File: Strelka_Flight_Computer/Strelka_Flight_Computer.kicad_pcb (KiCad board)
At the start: 4 copper layers, 91 x 30.1 mm, 174 parts, among them IC1 XTSD04GLGEAG, IC2 MAX-M10S-00B, J2 Conn_01x04, J3 DB125-3.5-4P-GN-S, J4 SM06B-GHS-TB(LF)(SN), J6 USB_B_Micro, J7 Conn_01x02, J8 Conn_01x07, Q1 CJK2333, Q10 AP2300, Q11 MMBT2222, Q15 AO3400A, Q16 AO3400A, Q17 AO3401A, Q2 CJK2333, Q4 AO3401A, Q5 AP2300, Q6 MMBT2222, Q9 AO3401A, SW1 SW_DIP_x01, SW6 TS-1185-C-A-A-A, SW7 TS-1185-C-A-A-A, U1 ASM330LHHXTR, U11 BMX055, U12 MS561101BA03-50, U16 TPS61085DGKR, U2 AP9101CK6, U3 AMS1117-3.3, U4 RFM95W-915S2, U5 MCP2551-I-SN, U6 STM32H743VITx, U8 USBLC6-2SC6, Y5 Q13FC1350000400, Y6 X1E0000210834

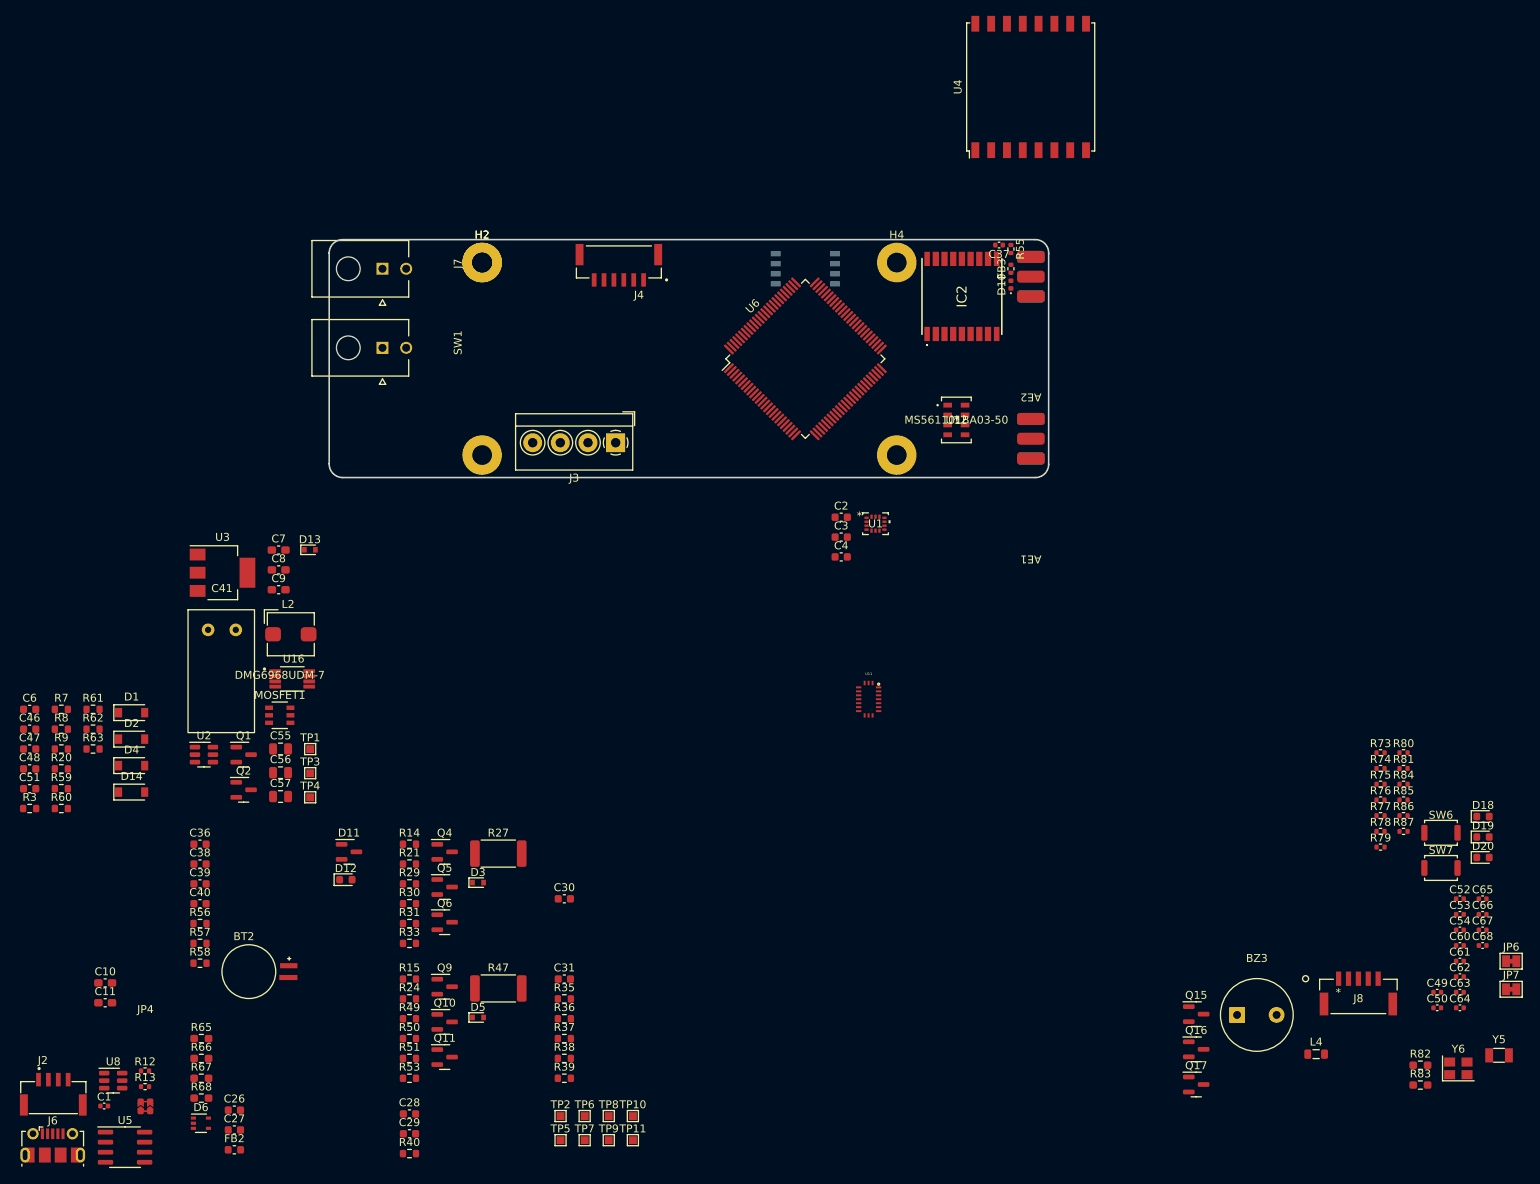
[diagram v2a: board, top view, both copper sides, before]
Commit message: Started component placement
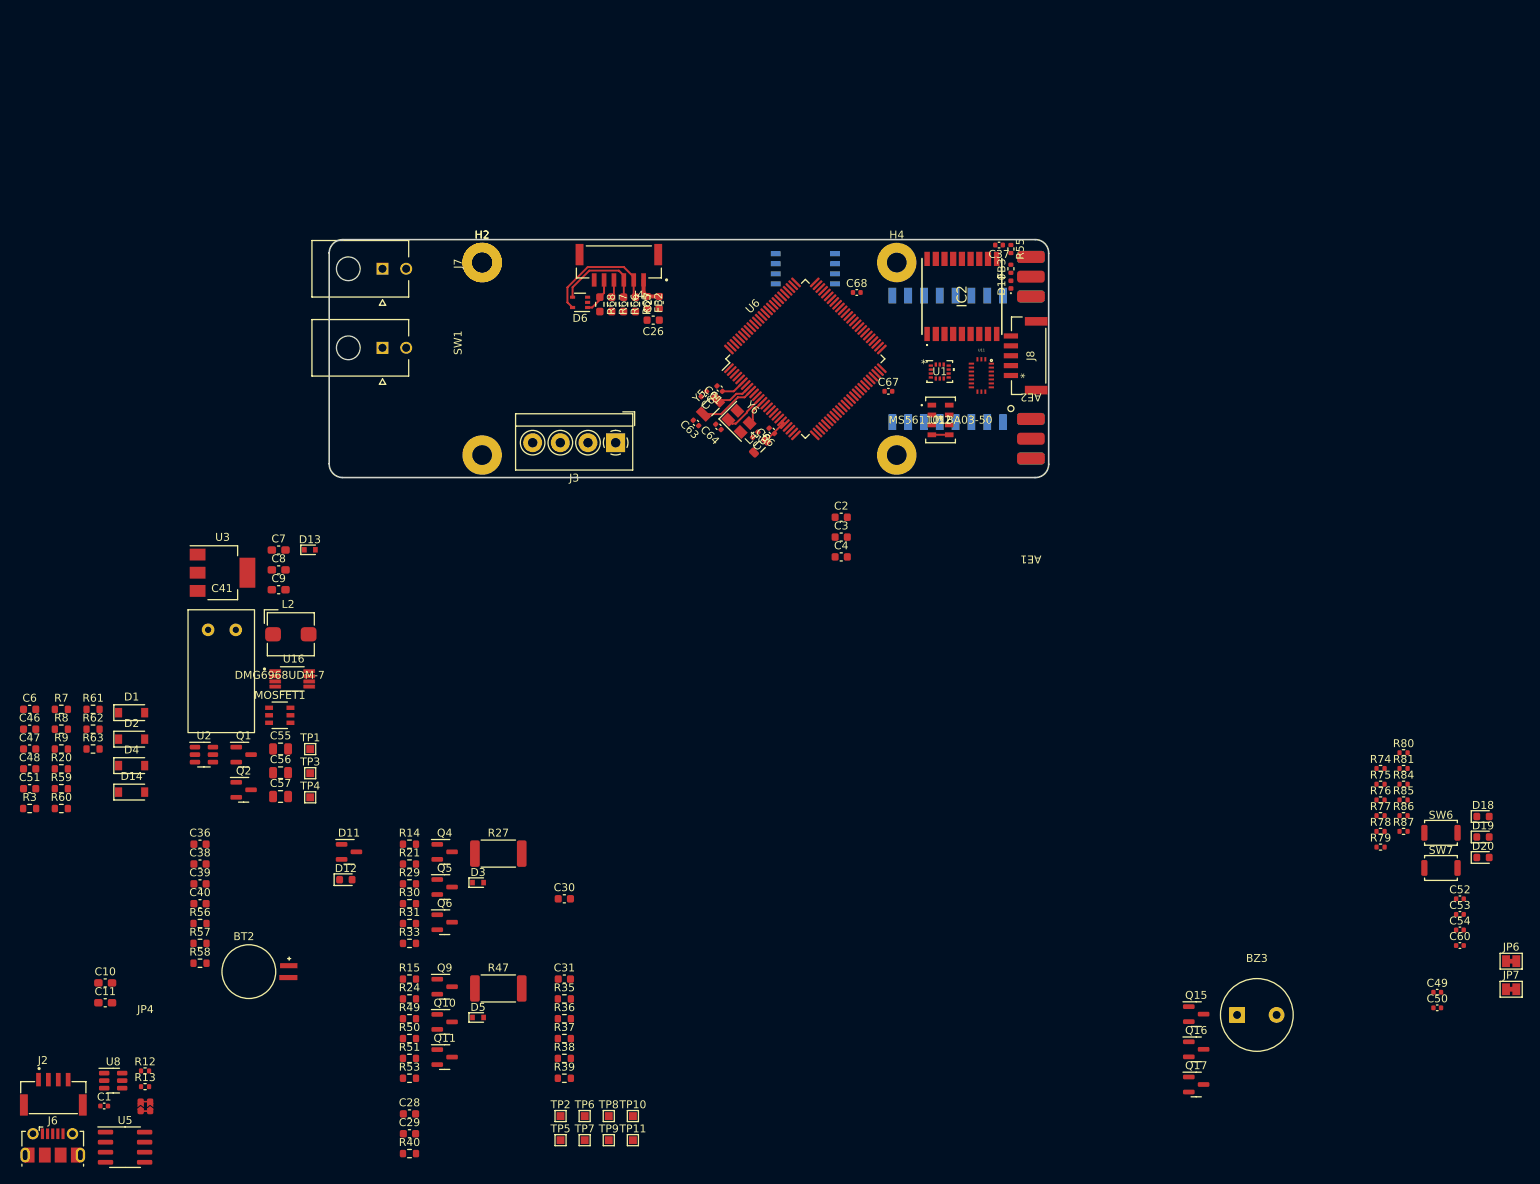
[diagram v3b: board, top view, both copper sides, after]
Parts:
- removed R73: 100k, Resistor_SMD:R_0402_1005Metric
- removed R82: NC, Resistor_SMD:R_0603_1608Metric_Pad0.98x0.95mm_HandSolder
- removed R83: 10k, Resistor_SMD:R_0603_1608Metric_Pad0.98x0.95mm_HandSolder
- U4: moved to B.Cu
- moved Y5 129.1 mm to (146.5, 69.5), turned to 45 degrees
- moved Y6 122.4 mm to (150.1, 71.3), turned to -45 degrees
- moved C62 120.7 mm to (145.7, 67.8), turned to -135 degrees
- moved C63 120.5 mm to (144.7, 71.5), turned to 135 degrees
- moved FB2 119.2 mm to (138.5, 56.3), turned to -90 degrees
- moved C64 119.2 mm to (147.5, 72.0), turned to 135 degrees
- moved C61 118.4 mm to (147.7, 67.2), turned to 135 degrees
- moved C27 117.7 mm to (140.0, 56.3), turned to 90 degrees
- moved C68 114.4 mm to (165.0, 55.0)
- moved D6 114.4 mm to (130.0, 56.2), turned to 180 degrees
- moved C26 113.1 mm to (139.2, 58.5), turned to 180 degrees
- moved R68 112.4 mm to (132.5, 56.5), turned to -90 degrees
- moved R67 110.8 mm to (134.0, 56.5), turned to -90 degrees
- moved R66 109.3 mm to (135.5, 56.5), turned to -90 degrees
- moved C65 109.1 mm to (152.2, 73.0), turned to -135 degrees
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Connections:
- C66 pad 1: Net-(U6-VDDA) -> /STM32H743/VDDA
- L4 pad 2: Net-(U6-VDDA) -> /STM32H743/VDDA
- U1 pad 4: /STM32H743/INT_IN4 -> /STM32H743/EXTI13
- U1 pad 9: /STM32H743/INT_IN5 -> /STM32H743/EXTI14
- U11 pad 14: /STM32H743/INT_IN2 -> /STM32H743/EXTI6
- U11 pad 19: /STM32H743/INT_IN1 -> /STM32H743/EXTI15
- U11 pad 2: /STM32H743/INT_IN3 -> /STM32H743/EXTI7
- U6 pad 15: unconnected-(U6-PC0-Pad15) -> GND
- U6 pad 21: Net-(U6-VDDA) -> /STM32H743/VDDA
- U6 pad 51: unconnected-(U6-PB12-Pad51) -> /915MHz_Radio/IO0_RF
- U6 pad 60: unconnected-(U6-PD13-Pad60) -> /STM32H743/EXTI13
- U6 pad 61: unconnected-(U6-PD14-Pad61) -> /STM32H743/EXTI14
- U6 pad 62: unconnected-(U6-PD15-Pad62) -> /STM32H743/EXTI15
- U6 pad 63: unconnected-(U6-PC6-Pad63) -> /STM32H743/EXTI6
- U6 pad 64: unconnected-(U6-PC7-Pad64) -> /STM32H743/EXTI7
- U6 pad 84: /STM32H743/INT_IN1 -> unconnected-(U6-PD3-Pad84)
- U6 pad 85: /STM32H743/INT_IN2 -> unconnected-(U6-PD4-Pad85)
- U6 pad 86: /STM32H743/INT_IN3 -> unconnected-(U6-PD5-Pad86)
- U6 pad 87: /STM32H743/INT_IN4 -> unconnected-(U6-PD6-Pad87)
- U6 pad 88: /STM32H743/INT_IN5 -> unconnected-(U6-PD7-Pad88)
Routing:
- net Net-(D6-K-Pad5): track 0.00 -> 15.4 mm
- net Net-(D6-K-Pad4): track 0.00 -> 11.6 mm
- net /STM32H743/OSC32_OUT: track 0.00 -> 7.28 mm
- net /STM32H743/OSC_IN: track 0.00 -> 5.52 mm
- net Net-(D6-K-Pad1): track 0.00 -> 4.69 mm
- net /STM32H743/OSC32_IN: track 0.00 -> 4.57 mm
- net /STM32H743/VDDA: track 0.00 -> 3.80 mm
- net Net-(C27-Pad2): track 0.00 -> 3.79 mm
- net /STM32H743/OSC_OUT: track 0.00 -> 3.36 mm
- net +3.3V: track 0.00 -> 3.08 mm
- net Net-(D6-K-Pad3): track 0.00 -> 2.30 mm
- net /STM32H743/SPI4_NSS: track 0.00 -> 2.20 mm

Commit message: Changed design rules
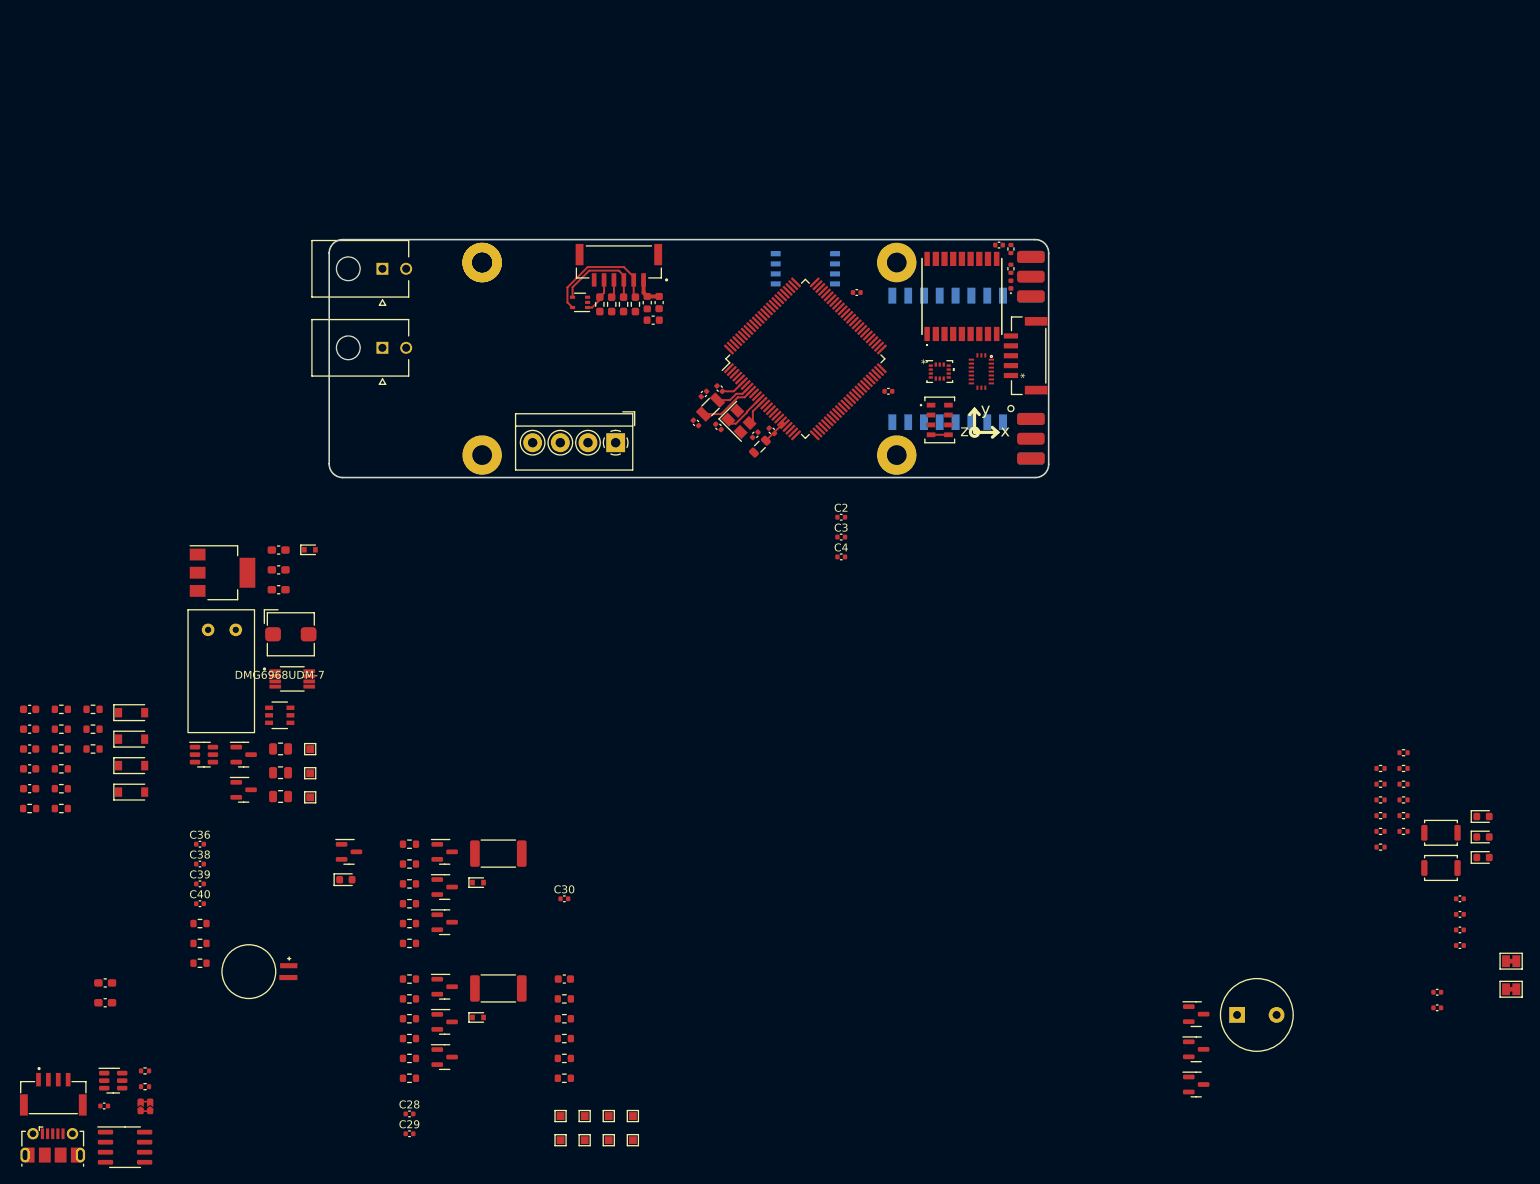
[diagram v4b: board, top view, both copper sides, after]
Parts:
- removed R40: 0R, Resistor_SMD:R_0603_1608Metric
- C2, C28, C29, C3, C30, C36, C38, C39, C4, C40: footprint Capacitor_SMD:C_0603_1608Metric -> Capacitor_SMD:C_0402_1005Metric
- moved U11 0.50 mm to (180.8, 65.0)
- moved U12 0.10 mm to (175.5, 71.1)
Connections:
- U11 pad 7: Net-(U11-PS) -> GND
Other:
- board text added: "x"
- board text added: "y"
- board text added: "z"

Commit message: Routing starting
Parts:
- removed C57: NC, Capacitor_SMD:C_0805_2012Metric
- removed C9: 10uF, Capacitor_SMD:C_0603_1608Metric_Pad1.08x0.95mm_HandSolder
- removed the H2 at (117.6, 51.2)
- removed R29, R30, R49, R50: 100k, Resistor_SMD:R_0603_1608Metric
- removed R33, R53: 1k, Resistor_SMD:R_0603_1608Metric
- removed R36, R37, R38, R39: 47k, Resistor_SMD:R_0603_1608Metric
- removed R58: 0R, Resistor_SMD:R_0603_1608Metric
- removed R66, R67, R68: 33, Resistor_SMD:R_0603_1608Metric_Pad0.98x0.95mm_HandSolder
- removed R85: 10R, Resistor_SMD:R_0402_1005Metric
- added C5: 100n, Capacitor_SMD:C_0402_1005Metric, F.Cu at (119.8, 56.0)
- added R1: NC, Resistor_SMD:R_0603_1608Metric, F.Cu at (146.9, 134.4)
- added R10: 1k, Resistor_SMD:R_0402_1005Metric, F.Cu at (136.6, 138.1)
- added R11: 1k, Resistor_SMD:R_0402_1005Metric, F.Cu at (141.5, 138.1)
- added R16: 1k, Resistor_SMD:R_0402_1005Metric, F.Cu at (136.6, 140.1)
- added R17: 1k, Resistor_SMD:R_0402_1005Metric, F.Cu at (130.9, 80.7)
- added R18: 33, Resistor_SMD:R_0402_1005Metric, F.Cu at (135.5, 55.7)
- added R19: 33, Resistor_SMD:R_0402_1005Metric, F.Cu at (134.3, 55.7)
- added R2: 100k, Resistor_SMD:R_0402_1005Metric, F.Cu at (136.6, 134.1)
- added R22: 10R, Resistor_SMD:R_0402_1005Metric, F.Cu at (162.4, 53.4)
- added R23: 47k, Resistor_SMD:R_0402_1005Metric, F.Cu at (155.4, 52.5)
- added R25: 47k, Resistor_SMD:R_0402_1005Metric, F.Cu at (165.0, 56.0)
- added R4: 100k, Resistor_SMD:R_0402_1005Metric, F.Cu at (141.5, 134.1)
- added R5: 100k, Resistor_SMD:R_0402_1005Metric, F.Cu at (136.6, 136.1)
- added R6: 100k, Resistor_SMD:R_0402_1005Metric, F.Cu at (141.5, 136.1)
- C31, C47: footprint Capacitor_SMD:C_0603_1608Metric -> Capacitor_SMD:C_0402_1005Metric
- C48: value 0.1u -> 100n; footprint Capacitor_SMD:C_0603_1608Metric -> Capacitor_SMD:C_0402_1005Metric
- C51: value 820p -> 2.2n; footprint Capacitor_SMD:C_0603_1608Metric -> Capacitor_SMD:C_0402_1005Metric
- C6: value 0.1uF -> 100n; footprint Capacitor_SMD:C_0603_1608Metric -> Capacitor_SMD:C_0402_1005Metric
- C7: value 100nF -> 10uF; footprint Capacitor_SMD:C_0603_1608Metric_Pad1.08x0.95mm_HandSolder -> Capacitor_SMD:C_0402_1005Metric
- C8: footprint Capacitor_SMD:C_0603_1608Metric_Pad1.08x0.95mm_HandSolder -> Capacitor_SMD:C_0402_1005Metric
- JP6, JP7: footprint Jumper:SolderJumper-2_P1.3mm_Bridged_Pad1.0x1.5mm -> Jumper:SolderJumper-2_P1.3mm_Bridged2Bar_RoundedPad1.0x1.5mm
- Q10, Q4, Q5, Q9, R27, R47, U5: moved to B.Cu
- R14, R15, R3, R31, R35, R51, R56, R57, R7, R8: footprint Resistor_SMD:R_0603_1608Metric -> Resistor_SMD:R_0402_1005Metric
- R20: value 0 -> 47k; footprint Resistor_SMD:R_0603_1608Metric -> Resistor_SMD:R_0402_1005Metric
- R21: value 1k -> 33; footprint Resistor_SMD:R_0603_1608Metric -> Resistor_SMD:R_0402_1005Metric
- R24: value 1k -> 47k; footprint Resistor_SMD:R_0603_1608Metric -> Resistor_SMD:R_0402_1005Metric
- R61: value 56.2k -> 10k; footprint Resistor_SMD:R_0603_1608Metric -> Resistor_SMD:R_0402_1005Metric
- R65: footprint Resistor_SMD:R_0603_1608Metric_Pad0.98x0.95mm_HandSolder -> Resistor_SMD:R_0402_1005Metric
- moved BZ3 113.8 mm to (148.0, 53.0), turned to 180 degrees
- moved J2 112.9 mm to (141.8, 75.6)
- moved R20 109.3 mm to (154.5, 53.4), turned to -45 degrees
- moved J6 96.9 mm to (101.3, 73.8), turned to -90 degrees
- moved C31 96.6 mm to (164.9, 52.5)
- moved R84 95.0 mm to (163.1, 54.1), turned to 45 degrees
- moved R35 93.5 mm to (153.6, 54.4), turned to -45 degrees
- moved U8 87.4 mm to (106.0, 74.7), turned to 90 degrees
- moved R3 87.1 mm to (113.7, 51.4), turned to 90 degrees
- moved C48 85.2 mm to (125.7, 60.5)
- moved C51 83.7 mm to (119.3, 58.4)
- moved D4 79.8 mm to (131.3, 60.1), turned to 90 degrees
- moved R24 78.6 mm to (158.8, 84.1)
- moved R8 78.3 mm to (125.7, 61.5)
- moved R63 77.5 mm to (122.9, 57.7), turned to 180 degrees
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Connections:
- net Net-(U6-PA11) renamed /STM32H743/D-
- C7 pad 1: +5V -> +3V3
- Q2 pad 3: Net-(Q2-D) -> +5VA
- R20 pad 1: +5VA -> +3V3
- R20 pad 2: Net-(Q2-D) -> /Data_Logging/SD3
- R21 pad 1: /Actuators/Ematch_Drogue1/EMATCH+ -> Net-(D6-K-Pad1)
- R21 pad 2: VDC -> /Actuators/EXT_SPI_CS
- R24 pad 1: /Actuators/Ematch_Main/EMATCH+ -> +3V3
- R24 pad 2: VDC -> /Data_Logging/SD1
- U6 pad 22: /STM32H743/GPS_PPS -> /Sensors/MAX-M10S-00B/PPS
- U6 pad 71: Net-(U6-PA12) -> /STM32H743/D+
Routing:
- net /Data_Interfaces/USB_D-: track 0.00 -> 75.3 mm, vias 0 -> 2
- net /Data_Interfaces/USB_D+: track 0.00 -> 75.2 mm, vias 0 -> 2
- net /STM32H743/GPS_RST: track 0.00 -> 40.0 mm, vias 0 -> 2
- net /915MHz_Radio/SPI_CLK: track 0.00 -> 34.6 mm, vias 0 -> 3
- net /Sensors/MAX-M10S-00B/PPS: track 0.00 -> 31.4 mm
- net /915MHz_Radio/SPI_MOSI: track 0.00 -> 30.4 mm, vias 0 -> 4
- net /915MHz_Radio/SPI_MISO: track 0.00 -> 30.2 mm, vias 0 -> 3
- net /STM32H743/USART2_TX: track 0.00 -> 29.0 mm
- net /STM32H743/USART2_RX: track 0.00 -> 27.0 mm
- net /Data_Logging/CMD: track 0.00 -> 19.0 mm, vias 0 -> 1
- net /STM32H743/SPI4_MOSI: track 0.00 -> 14.1 mm, vias 0 -> 2
- net /STM32H743/SPI4_MISO: track 0.00 -> 13.4 mm, vias 0 -> 2
- net /STM32H743/SPI4_NSS: track 2.20 -> 15.0 mm, vias 0 -> 2
- net /STM32H743/SPI4_SCK: track 0.00 -> 12.4 mm, vias 0 -> 2
- net /Data_Logging/SD0: track 0.00 -> 9.03 mm, vias 0 -> 1
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- added copper zone on F.Cu, net Net-(D14-A)
- added copper zone on F.Cu, net VDC

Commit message: Continued routing
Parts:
- added F1: MF-PSHT035KX-2, Resistor_SMD:R_0805_2012Metric, F.Cu at (138.4, 70.3)
- R1: value NC -> 0R
- moved JP4 113.6 mm to (142.0, 66.2)
- moved D18 107.5 mm to (147.8, 73.8), turned to 180 degrees
- moved R13 107.1 mm to (141.8, 71.7)
- moved R12 105.8 mm to (140.2, 70.2), turned to -90 degrees
- moved Q15 91.9 mm to (148.4, 76.3)
- moved R76 91.0 mm to (150.9, 76.5), turned to 90 degrees
- moved R87 89.7 mm to (171.2, 59.4), turned to 180 degrees
- moved R86 89.1 mm to (171.2, 58.2), turned to 180 degrees
- moved R74 87.3 mm to (152.4, 77.7)
- moved U5 48.9 mm to (141.8, 66.9), turned to -90 degrees
- moved R24 29.5 mm to (164.1, 55.1), turned to -135 degrees
- moved C4 25.8 mm to (177.5, 67.1)
- moved C2 23.2 mm to (177.9, 65.6), turned to 90 degrees
- moved C3 22.6 mm to (175.6, 67.1)
- moved C31 4.04 mm to (160.9, 52.0), turned to 45 degrees
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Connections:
- net /Data_Interfaces/CAN_RXD renamed /Data_Interfaces/CAN_N
- net /Data_Interfaces/CAN_TXD renamed /Data_Interfaces/CAN_P
- net Net-(AE1-A) renamed /915MHz_Radio/LoRa_Sig
- net Net-(D1-K) renamed /Power/SW_IN
- C2 pad 1: +3V3 -> +3.3V
- C28 pad 1: +3V3 -> +3.3V
- C29 pad 1: +3V3 -> +3.3V
- C3 pad 1: +3V3 -> +3.3V
- C30 pad 1: +3V3 -> +3.3V
- C31 pad 1: +3V3 -> +3.3V
- C4 pad 1: +3V3 -> +3.3V
- IC1 pad 8: +3V3 -> +3.3V
- J2 pad 1: GND -> /Data_Interfaces/V_CAN
- R20 pad 1: +3V3 -> +3.3V
- R23 pad 1: +3V3 -> +3.3V
- R24 pad 1: +3V3 -> +3.3V
- R25 pad 1: +3V3 -> +3.3V
- R35 pad 1: +3V3 -> +3.3V
- U1 pad 5: +3V3 -> +3.3V
- U1 pad 8: +3V3 -> +3.3V
- U11 pad 13: +3V3 -> +3.3V
- U11 pad 3: +3V3 -> +3.3V
- U12 pad 1: +3V3 -> +3.3V
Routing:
- net +5V: track 0.00 -> 48.3 mm, vias 0 -> 2
- net VBUS: track 2.78 -> 43.3 mm, vias 0 -> 4
- net /Actuators/EXT_SPI_CS: track 0.00 -> 35.0 mm, vias 0 -> 2
- net /Actuators/EXT_SPI_SCK: track 0.00 -> 34.2 mm, vias 0 -> 2
- net /Actuators/EXT_SPI_MOSI: track 0.00 -> 34.0 mm, vias 0 -> 2
- net /Actuators/EXT_SPI_MISO: track 0.00 -> 32.7 mm, vias 0 -> 2
- net /STM32H743/SPI2_NSS3: track 0.00 -> 30.2 mm, vias 0 -> 2
- net /STM32H743/I2C2_SCL: track 0.00 -> 28.2 mm, vias 0 -> 2
- net /STM32H743/I2C2_SDA: track 0.00 -> 24.7 mm, vias 0 -> 2
- net /STM32H743/SPI2_NSS2: track 0.00 -> 24.3 mm, vias 0 -> 2
- net +3.3V: track 3.08 -> 27.2 mm, vias 0 -> 10
- net /STM32H743/EXTI7: track 0.00 -> 23.7 mm, vias 0 -> 2
- net /STM32H743/EXTI15: track 0.00 -> 20.3 mm, vias 0 -> 2
- net /STM32H743/EXTI6: track 0.00 -> 19.8 mm, vias 0 -> 2
- net /Data_Interfaces/CAN_N: track 0.00 -> 16.9 mm
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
